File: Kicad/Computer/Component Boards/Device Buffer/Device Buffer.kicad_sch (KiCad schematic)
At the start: 20 parts, among them IC1 SN74ABT245BDBR, IC2 SN74ABT245BDBR, IC3 SN74ABT245BDBR, IC4 SN74ABT245BDBR, IC5 AP7365-33WG-7, J2 Conn_02x32_Counter_Clockwise

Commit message: Auto-routed VIA and Sound Boards (again).
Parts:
- removed RN5, RN6: CAY16-102J4LF, SamacSys_Parts:CAY16-J4, symbol Bourns:CAY16-102J4LF
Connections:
- net Device ~{CS}: now also IC3.13 (B5), J2.64 (Pin_64); no longer IC3.19 (~{OE}), J2.1 (Pin_1)
- net GND: now also IC3.19 (~{OE}), IC3.8 (A6); no longer IC3.5 (A3), IC3.7 (A5)
- net S: now also IC3.15 (B3); no longer IC3.12 (B6)
- net S_{IN}: now also IC3.5 (A3); no longer IC3.8 (A6)
- net ~{RD}_{OUT}: now also IC4.1 (DIR); no longer IC3.18 (B0), J2.54 (Pin_54)
- removed net DIR: IC4.1 (DIR), J2.64 (Pin_64)
- net ~{WD}_{OUT} renamed ~{WD}
- new net Device ~{CS}_{IN}: IC3.7 (A5), J2.1 (Pin_1)
- new net ~{RD}: IC3.18 (B0), J2.54 (Pin_54)
- no-connect marks 1 -> 4

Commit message: Standardising DIP board layouts.
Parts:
- J2: footprint SamacSys_Parts:DIP-64_Board_W15.24mm -> (none)
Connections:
- net ~{RD}_{OUT} is gone; now on net ~{RD}: IC4.1 (DIR)
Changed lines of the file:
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@@
+    (effects (font (size 1.27 1.27)) (justify right bottom))
+  )
+  (label "~{RD}" (at 187.325 34.925 180) (fields_autoplaced)
     (effects (font (size 1.27 1.27)) (justify right bottom))
   )
@@
   )
   (label "5V" (at 21.59 32.385 180) (fields_autoplaced)
-    (effects (font (size 1.27 1.27)) (justify right bottom))
-  )
-  (label "~{RD}_{OUT}" (at 187.325 34.925 180) (fields_autoplaced)
     (effects (font (size 1.27 1.27)) (justify right bottom))
   )
@@
       (effects (font (size 1.27 1.27)))
     )
-    (property "Footprint" "SamacSys_Parts:DIP-64_Board_W15.24mm" (at 34.925 127.635 0)
-      (effects (font (size 1.27 1.27)) hide)
-    )
+    (property "Footprint" "" (at 34.925 127.635 0)
+      (effects (font (size 1.27 1.27)) hide)
+    )

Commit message: Resized 15mm wide boards and fixed GND pins.  Added GPIO 4bit and PS2 Board.
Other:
- title: 8bit Data 8bit Signal Buffer -> Device Buffer
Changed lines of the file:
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@@
   (paper "A4")
   (title_block
-    (title "8bit Data 8bit Signal Buffer")
+    (title "Device Buffer")
     (date "2023-10-07")
     (rev "V0")

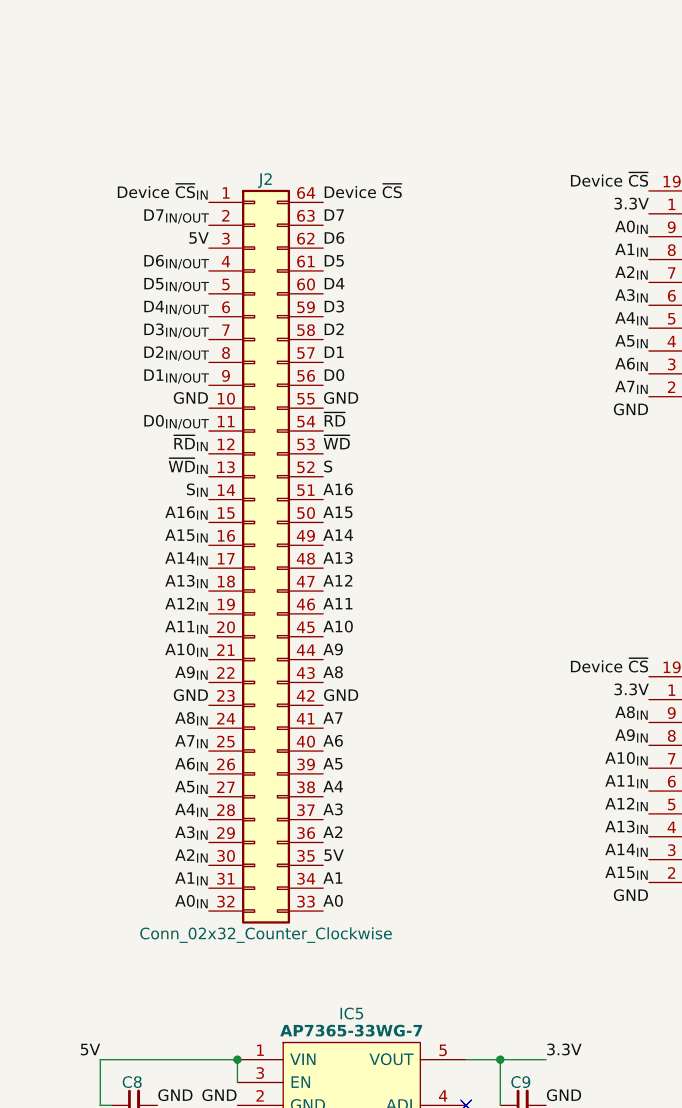
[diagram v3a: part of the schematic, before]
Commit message: Added a Test MPU Board and reversed the Device Buffer.
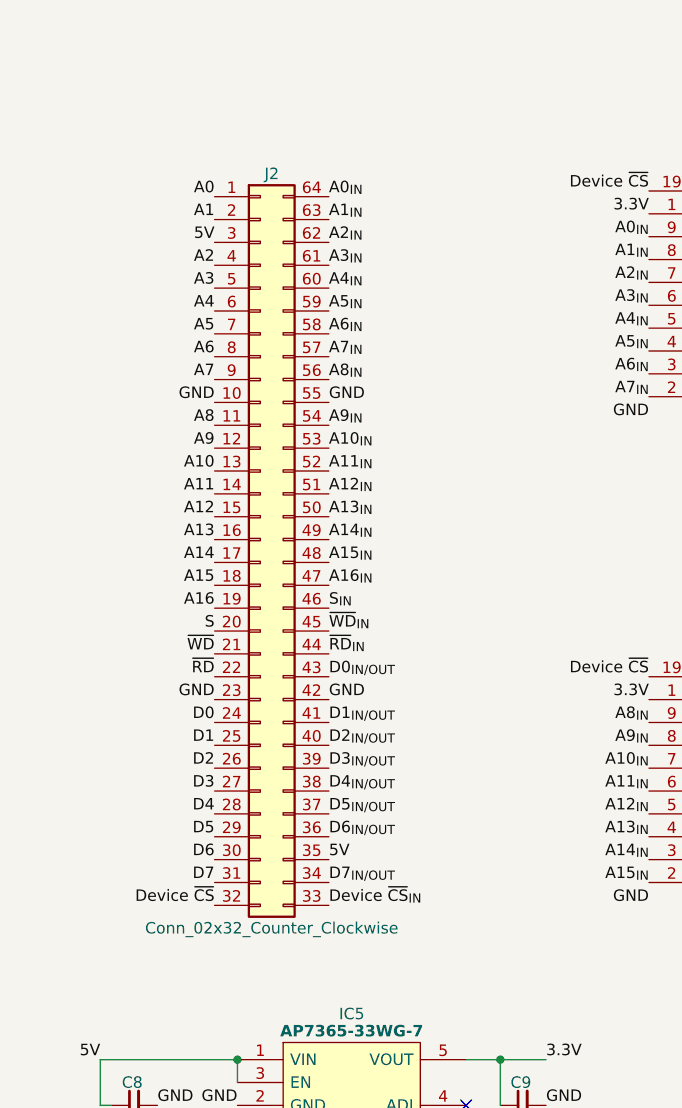
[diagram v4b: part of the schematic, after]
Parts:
- J2: footprint (none) -> SamacSys_Parts:DIP-64_Board_W15.24mm
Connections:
- net A0: now also J2.1 (Pin_1); no longer J2.33 (Pin_33)
- net A0_{IN}: now also J2.64 (Pin_64); no longer J2.32 (Pin_32)
- net A1: now also J2.2 (Pin_2); no longer J2.34 (Pin_34)
- net A10: now also J2.13 (Pin_13); no longer J2.45 (Pin_45)
- net A10_{IN}: now also J2.53 (Pin_53); no longer J2.21 (Pin_21)
- net A11: now also J2.14 (Pin_14); no longer J2.46 (Pin_46)
- net A11_{IN}: now also J2.52 (Pin_52); no longer J2.20 (Pin_20)
- net A12: now also J2.15 (Pin_15); no longer J2.47 (Pin_47)
- net A12_{IN}: now also J2.51 (Pin_51); no longer J2.19 (Pin_19)
- net A13: now also J2.16 (Pin_16); no longer J2.48 (Pin_48)
- net A13_{IN}: now also J2.50 (Pin_50); no longer J2.18 (Pin_18)
- net A14: now also J2.17 (Pin_17); no longer J2.49 (Pin_49)
- net A14_{IN}: now also J2.49 (Pin_49); no longer J2.17 (Pin_17)
- net A15: now also J2.18 (Pin_18); no longer J2.50 (Pin_50)
- net A15_{IN}: now also J2.48 (Pin_48); no longer J2.16 (Pin_16)
- net A16: now also J2.19 (Pin_19); no longer J2.51 (Pin_51)
- net A16_{IN}: now also J2.47 (Pin_47); no longer J2.15 (Pin_15)
- net A1_{IN}: now also J2.63 (Pin_63); no longer J2.31 (Pin_31)
- net A2: now also J2.4 (Pin_4); no longer J2.36 (Pin_36)
- net A2_{IN}: now also J2.62 (Pin_62); no longer J2.30 (Pin_30)
- net A3: now also J2.5 (Pin_5); no longer J2.37 (Pin_37)
- net A3_{IN}: now also J2.61 (Pin_61); no longer J2.29 (Pin_29)
- net A4: now also J2.6 (Pin_6); no longer J2.38 (Pin_38)
- net A4_{IN}: now also J2.60 (Pin_60); no longer J2.28 (Pin_28)
- net A5: now also J2.7 (Pin_7); no longer J2.39 (Pin_39)
- net A5_{IN}: now also J2.59 (Pin_59); no longer J2.27 (Pin_27)
- net A6: now also J2.8 (Pin_8); no longer J2.40 (Pin_40)
- net A6_{IN}: now also J2.58 (Pin_58); no longer J2.26 (Pin_26)
- net A7: now also J2.9 (Pin_9); no longer J2.41 (Pin_41)
- net A7_{IN}: now also J2.57 (Pin_57); no longer J2.25 (Pin_25)
- net A8: now also J2.11 (Pin_11); no longer J2.43 (Pin_43)
- net A8_{IN}: now also J2.56 (Pin_56); no longer J2.24 (Pin_24)
- net A9: now also J2.12 (Pin_12); no longer J2.44 (Pin_44)
- net A9_{IN}: now also J2.54 (Pin_54); no longer J2.22 (Pin_22)
- net D0: now also J2.24 (Pin_24); no longer J2.56 (Pin_56)
- net D0_{IN/OUT}: now also J2.43 (Pin_43); no longer J2.11 (Pin_11)
- net D1: now also J2.25 (Pin_25); no longer J2.57 (Pin_57)
- net D1_{IN/OUT}: now also J2.41 (Pin_41); no longer J2.9 (Pin_9)
- net D2: now also J2.26 (Pin_26); no longer J2.58 (Pin_58)
- net D2_{IN/OUT}: now also J2.40 (Pin_40); no longer J2.8 (Pin_8)
- net D3: now also J2.27 (Pin_27); no longer J2.59 (Pin_59)
- net D3_{IN/OUT}: now also J2.39 (Pin_39); no longer J2.7 (Pin_7)
- net D4: now also J2.28 (Pin_28); no longer J2.60 (Pin_60)
- net D4_{IN/OUT}: now also J2.38 (Pin_38); no longer J2.6 (Pin_6)
- net D5: now also J2.29 (Pin_29); no longer J2.61 (Pin_61)
- net D5_{IN/OUT}: now also J2.37 (Pin_37); no longer J2.5 (Pin_5)
- net D6: now also J2.30 (Pin_30); no longer J2.62 (Pin_62)
- net D6_{IN/OUT}: now also J2.36 (Pin_36); no longer J2.4 (Pin_4)
- net D7: now also J2.31 (Pin_31); no longer J2.63 (Pin_63)
- net D7_{IN/OUT}: now also J2.34 (Pin_34); no longer J2.2 (Pin_2)
- net Device ~{CS}: now also J2.32 (Pin_32); no longer J2.64 (Pin_64)
- net Device ~{CS}_{IN}: now also J2.33 (Pin_33); no longer J2.1 (Pin_1)
- net S: now also J2.20 (Pin_20); no longer J2.52 (Pin_52)
- net S_{IN}: now also J2.46 (Pin_46); no longer J2.14 (Pin_14)
- net ~{RD}: now also J2.22 (Pin_22); no longer J2.54 (Pin_54)
- net ~{RD}_{IN}: now also J2.44 (Pin_44); no longer J2.12 (Pin_12)
- net ~{WD}: now also J2.21 (Pin_21); no longer J2.53 (Pin_53)
- net ~{WD}_{IN}: now also J2.45 (Pin_45); no longer J2.13 (Pin_13)
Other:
- moved on the sheet: J2

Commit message: Generating more Gerbers.
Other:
- moved on the sheet: C1, C3, C4, C5, C8, C9, IC1, IC3, IC4, IC5, RN1, RN2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

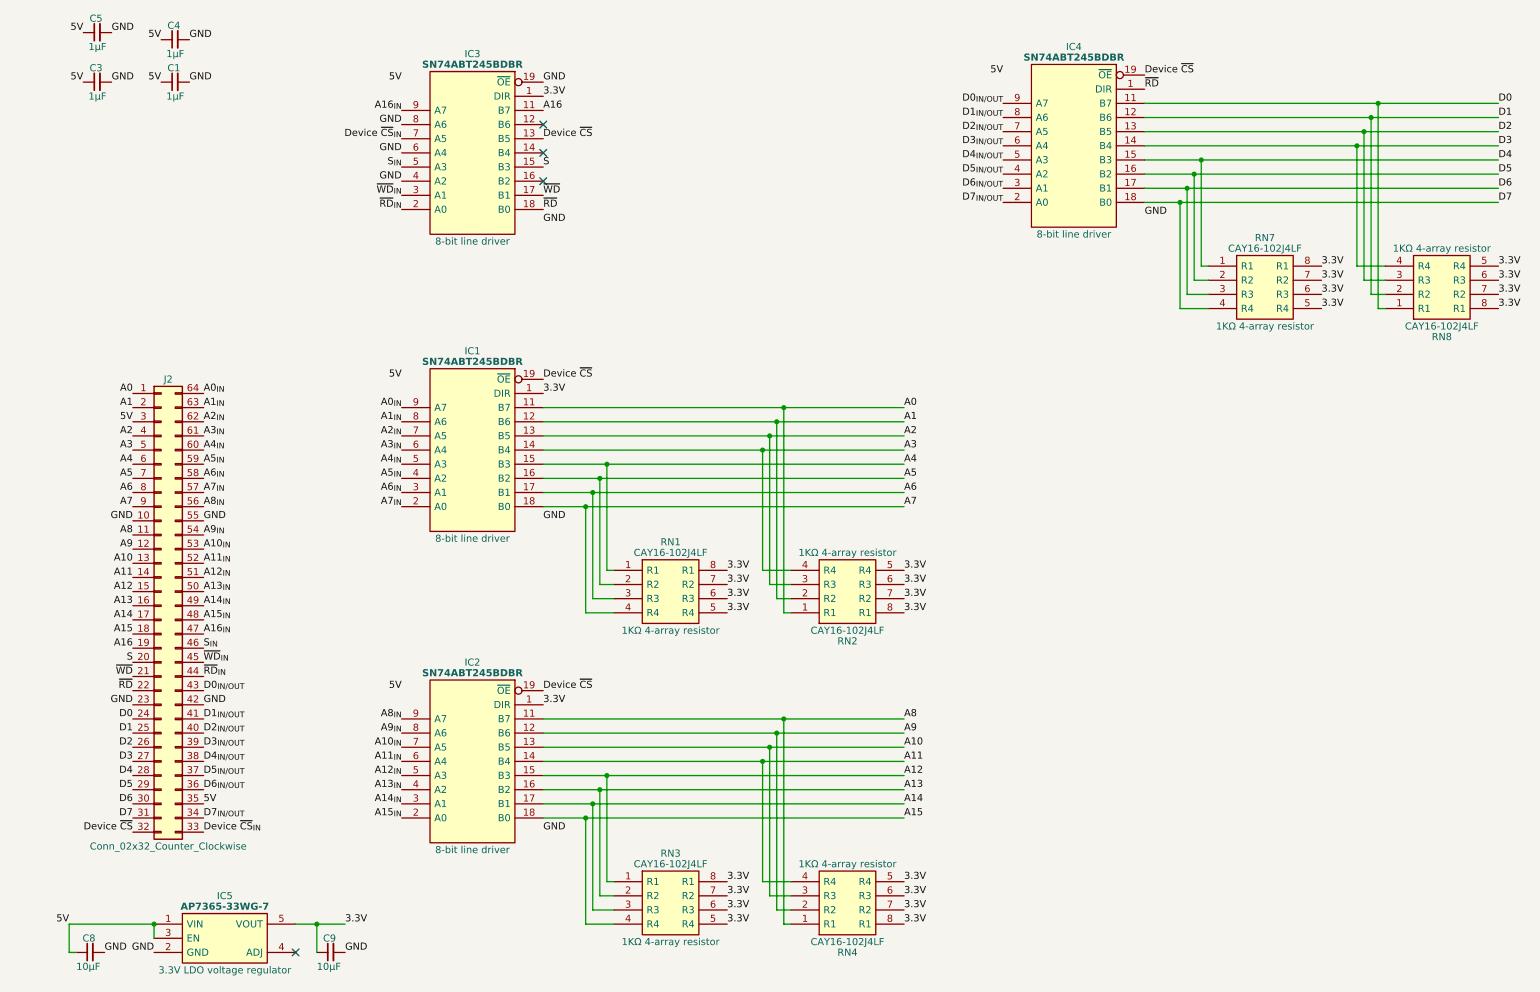
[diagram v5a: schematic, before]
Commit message: Cleaned up Device Buffer.
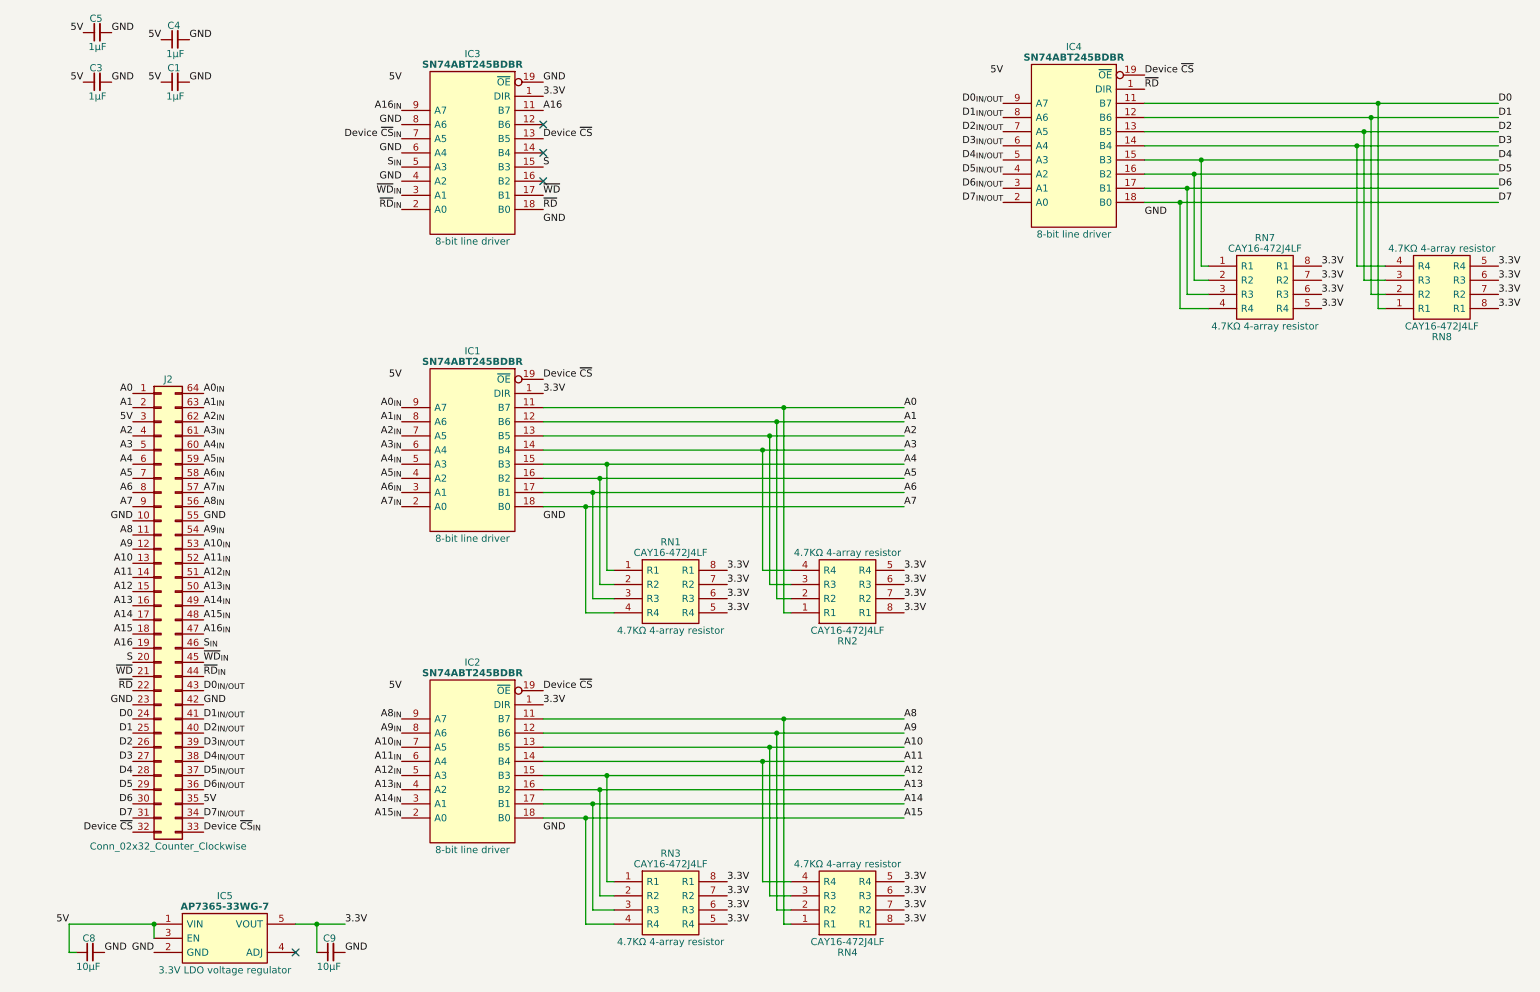
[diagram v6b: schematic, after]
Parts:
- RN1, RN2, RN3, RN4, RN7, RN8: value CAY16-102J4LF -> CAY16-472J4LF; footprint SamacSys_Parts:CAY16-J4 -> CAY16472J4LF; symbol Bourns:CAY16-102J4LF -> Bourns:CAY16-472J4LF; Manufacturer_Part_Number CAY16-102J4LF -> CAY16-472J4LF; Mouser Part Number 652-CAY16-102J4LF -> 652-CAY16-472J4LF; Silkscreen 1KΩ -> 4.7KΩ

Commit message: Regenerating some gerbers again with paste layers.
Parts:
- RN1, RN2, RN3, RN4, RN7, RN8: footprint CAY16472J4LF -> SamacSys_Parts:CAY16-F4
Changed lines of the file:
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@@
       (effects (font (size 1.27 1.27)))
     )
-    (property "Footprint" "CAY16472J4LF" (at 168.91 104.775 0)
+    (property "Footprint" "SamacSys_Parts:CAY16-F4" (at 168.91 104.775 0)
       (effects (font (size 1.27 1.27)) (justify left) hide)
     )
@@
       (effects (font (size 1.27 1.27)) (justify left) hide)
     )
-    (property "Silkscreen" "4.7KΩ" (at 172.085 99.695 0)
+    (property "Silkscreen" "4.7KΩ" (at 158.75 114.935 0)
       (effects (font (size 1.27 1.27)) hide)
     )
@@
       (effects (font (size 1.27 1.27)))
     )
-    (property "Footprint" "CAY16472J4LF" (at 243.84 89.535 0)
+    (property "Footprint" "SamacSys_Parts:CAY16-F4" (at 243.84 89.535 0)
       (effects (font (size 1.27 1.27)) (justify left) hide)
     )
@@
       (effects (font (size 1.27 1.27)) (justify left) hide)
     )
-    (property "Silkscreen" "4.7KΩ" (at 247.015 94.615 0)
+    (property "Silkscreen" "4.7KΩ" (at 233.68 79.375 0)
       (effects (font (size 1.27 1.27)) hide)
     )
@@
       (effects (font (size 1.27 1.27)))
     )
-    (property "Footprint" "CAY16472J4LF" (at 168.91 160.655 0)
+    (property "Footprint" "SamacSys_Parts:CAY16-F4" (at 168.91 160.655 0)
       (effects (font (size 1.27 1.27)) (justify left) hide)
     )
@@
       (effects (font (size 1.27 1.27)) (justify left) hide)
     )
-    (property "Silkscreen" "4.7KΩ" (at 172.085 155.575 0)
+    (property "Silkscreen" "4.7KΩ" (at 158.75 170.815 0)
       (effects (font (size 1.27 1.27)) hide)
     )
@@
       (effects (font (size 1.27 1.27)))
     )
-    (property "Footprint" "CAY16472J4LF" (at 137.16 200.025 0)
+    (property "Footprint" "SamacSys_Parts:CAY16-F4" (at 137.16 200.025 0)
       (effects (font (size 1.27 1.27)) (justify left) hide)
     )
@@
       (effects (font (size 1.27 1.27)) (justify left) hide)
     )
-    (property "Silkscreen" "4.7KΩ" (at 140.335 205.105 0)
+    (property "Silkscreen" "4.7KΩ" (at 127 189.865 0)
       (effects (font (size 1.27 1.27)) hide)
     )
@@
       (effects (font (size 1.27 1.27)))
     )
-    (property "Footprint" "CAY16472J4LF" (at 275.59 50.165 0)
+    (property "Footprint" "SamacSys_Parts:CAY16-F4" (at 275.59 50.165 0)
       (effects (font (size 1.27 1.27)) (justify left) hide)
     )
@@
       (effects (font (size 1.27 1.27)) (justify left) hide)
     )
-    (property "Silkscreen" "4.7KΩ" (at 278.765 45.085 0)
+    (property "Silkscreen" "4.7KΩ" (at 265.43 60.325 0)
       (effects (font (size 1.27 1.27)) hide)
     )
@@
       (effects (font (size 1.27 1.27)))
     )
-    (property "Footprint" "CAY16472J4LF" (at 137.16 144.145 0)
+    (property "Footprint" "SamacSys_Parts:CAY16-F4" (at 137.16 144.145 0)
       (effects (font (size 1.27 1.27)) (justify left) hide)
     )
@@
       (effects (font (size 1.27 1.27)) (justify left) hide)
     )
-    (property "Silkscreen" "4.7KΩ" (at 140.335 149.225 0)
-      (effects (font (size 1.27 1.27)) hide)
-    )
+    (property "Silkscreen" "4.7KΩ" (at 127 133.985 0)
+      (effects (font (size 1.27 1.27)) hide)
+    )
